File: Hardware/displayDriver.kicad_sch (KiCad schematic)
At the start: 22 parts, among them J3 Conn_01x10, J4 Conn_01x10, U10 4511, U11 HDSP-816E, U12 4511, U13 HDSP-816E, U6 4511, U7 HDSP-816E, U8 4511, U9 HDSP-816E

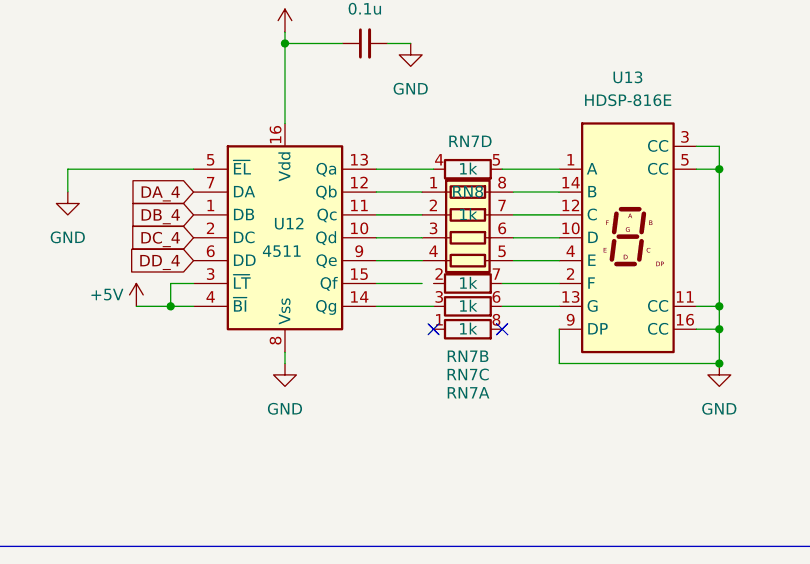
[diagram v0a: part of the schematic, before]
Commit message: Route the 10/hours digits. Update HDSP-816E footprint to include 3D representation
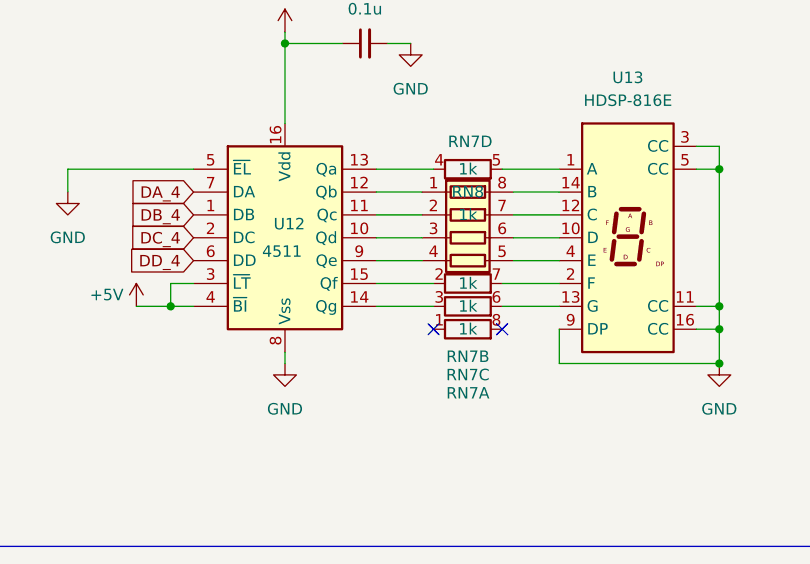
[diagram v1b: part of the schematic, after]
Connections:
- net at U12.15 (Qf): now also RN7.2 (R2.1)
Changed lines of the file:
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@@
 	(wire
 		(pts
-			(xy 78.74 138.43) (xy 83.82 138.43)
+			(xy 78.74 138.43) (xy 85.09 138.43)
 		)
 		(stroke

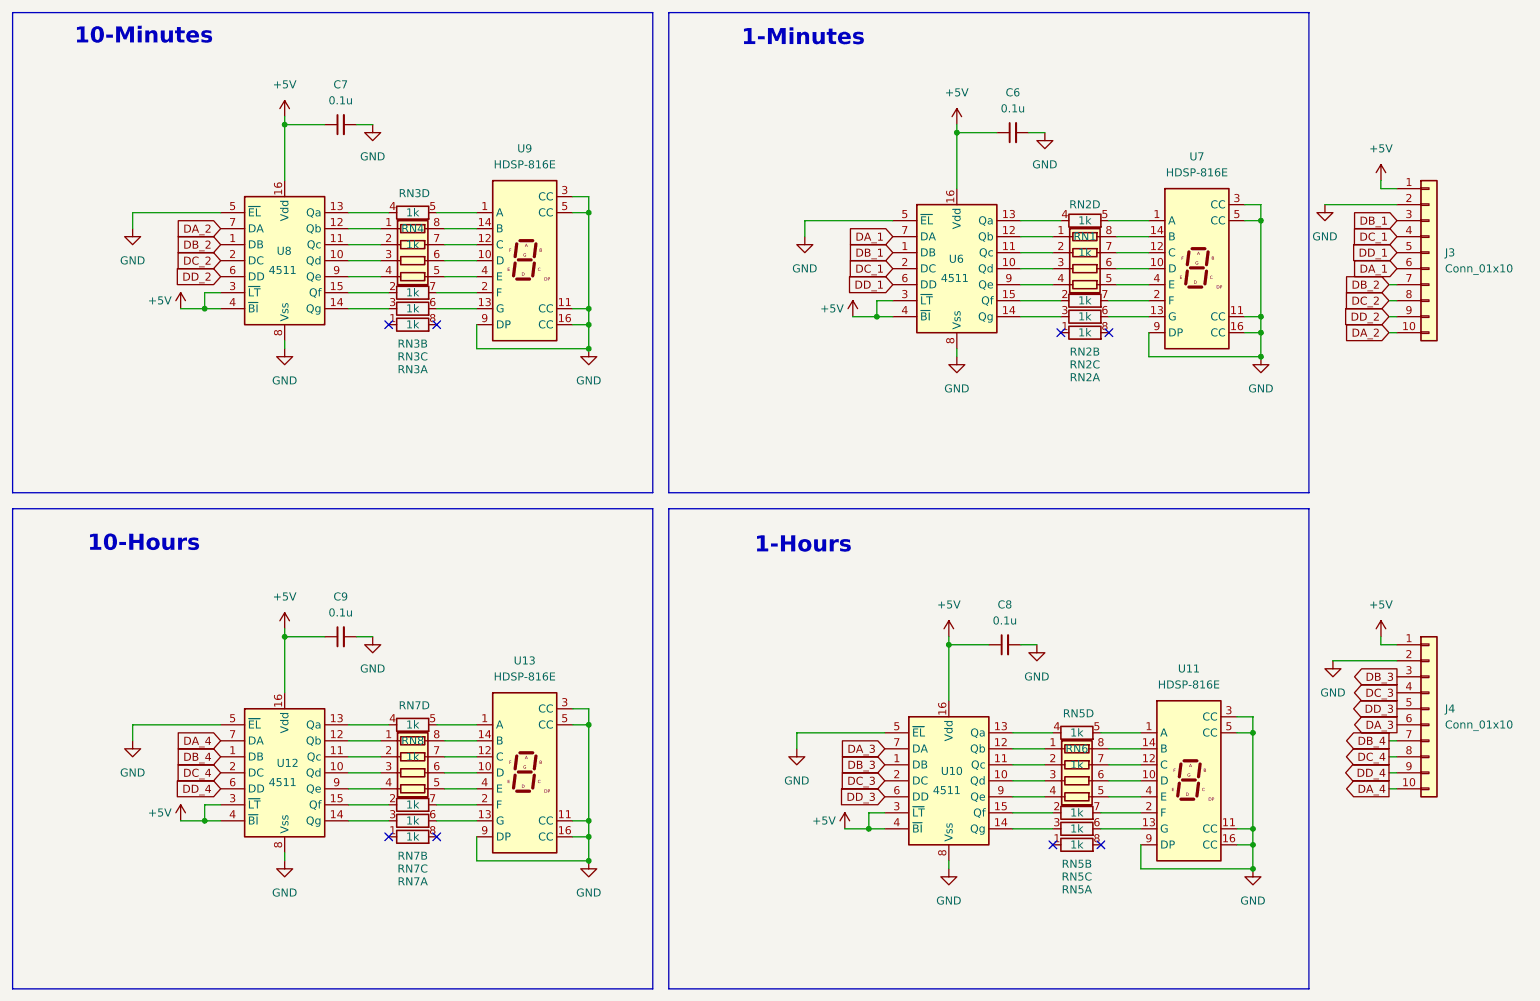
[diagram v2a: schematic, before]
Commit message: Make the IC changes for minute and hour counters
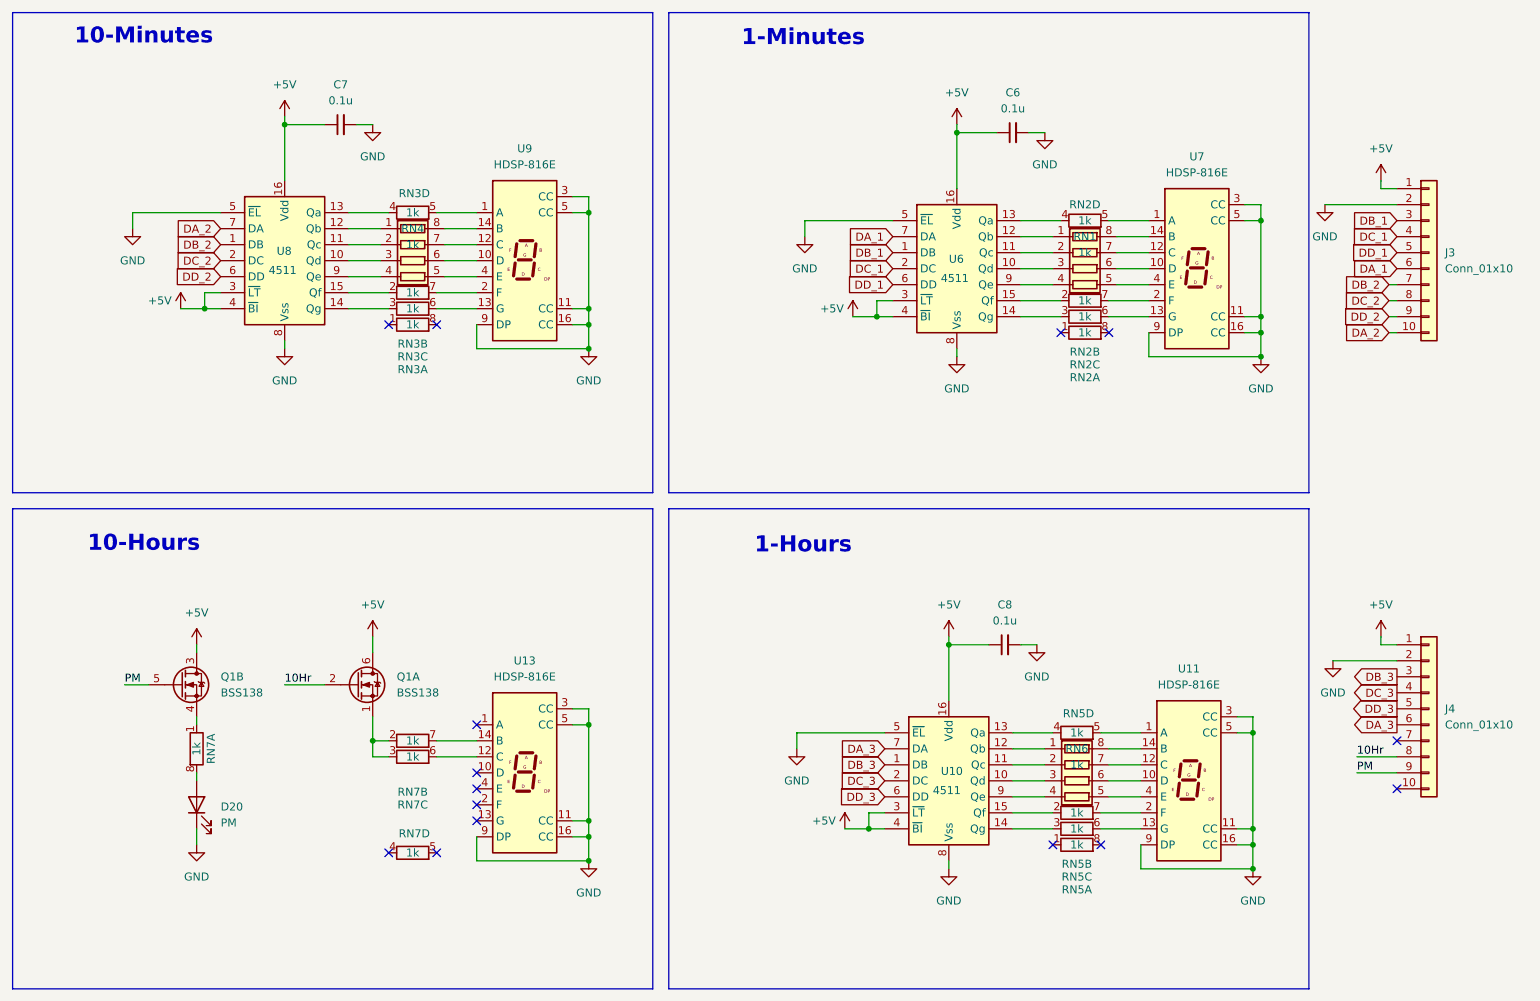
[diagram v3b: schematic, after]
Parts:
- removed C9: 0.1u, Capacitor_SMD:C_0603_1608Metric, symbol Device:C_Small
- removed RN8: 1k, Resistor_SMD:R_Array_Convex_4x0603, symbol Device:R_Pack04
- removed U12: 4511, Package_SO:TSSOP-16_4.4x5mm_P0.65mm, symbol 4xxx_IEEE:4511
- added D20: PM, LED_THT:LED_D5.0mm, symbol Device:LED
- added Q1: BSS138, Package_TO_SOT_SMD:SOT-363, symbol JKC_library:BSS138_dual
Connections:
- net +5V: now also Q1.3 (D2), Q1.6 (D1)
- net GND: now also D20.1 (K)
- net at U13.1 (A): no longer RN7.5 (R4.2)
- net at U13.12 (C): now also RN7.6 (R3.2)
- net at U13.13 (G): no longer RN7.6 (R3.2)
- net at U13.14 (B): now also RN7.7 (R2.2)
- net at U13.2 (F): no longer RN7.7 (R2.2)
- net at RN7.1 (R1.1): now also Q1.4 (S2)
- net at RN7.8 (R1.2): now also D20.2 (A)
- net at RN7.3 (R3.1): now also RN7.2 (R2.1), Q1.1 (S1)
- net DA_4: no longer names the net of J4.10 (Pin_10)
- net DB_4: no longer names the net of J4.7 (Pin_7)
- net DC_4 renamed 10Hr
- net 10Hr: now also Q1.2 (G1)
- net DD_4 renamed PM
- net PM: now also Q1.5 (G2)
- no-connect marks 8 -> 15
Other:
- moved on the sheet: RN7A, RN7B, RN7C

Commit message: Update component symbols and footpints
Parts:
- Q1: footprint Package_TO_SOT_SMD:SOT-363 -> Package_TO_SOT_SMD:SOT-363_SC-70-6
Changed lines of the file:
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@@
 			)
 		)
-		(property "Footprint" "Package_TO_SOT_SMD:SOT-363"
+		(property "Footprint" "Package_TO_SOT_SMD:SOT-363_SC-70-6"
 			(at 57.15 121.285 0)
 			(effects
@@
 			)
 		)
-		(property "Footprint" "Package_TO_SOT_SMD:SOT-363"
+		(property "Footprint" "Package_TO_SOT_SMD:SOT-363_SC-70-6"
 			(at 85.09 121.285 0)
 			(effects

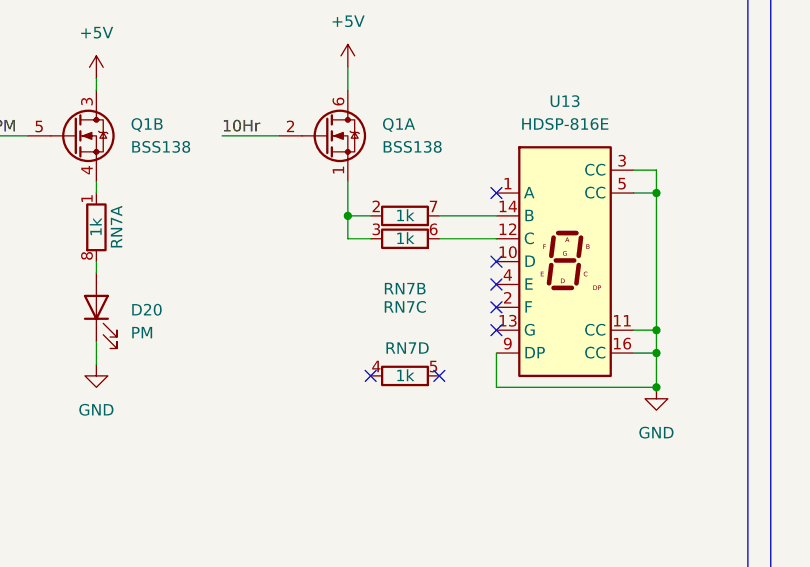
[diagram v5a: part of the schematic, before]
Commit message: Convert layout to 3 board design (power/logic/display)
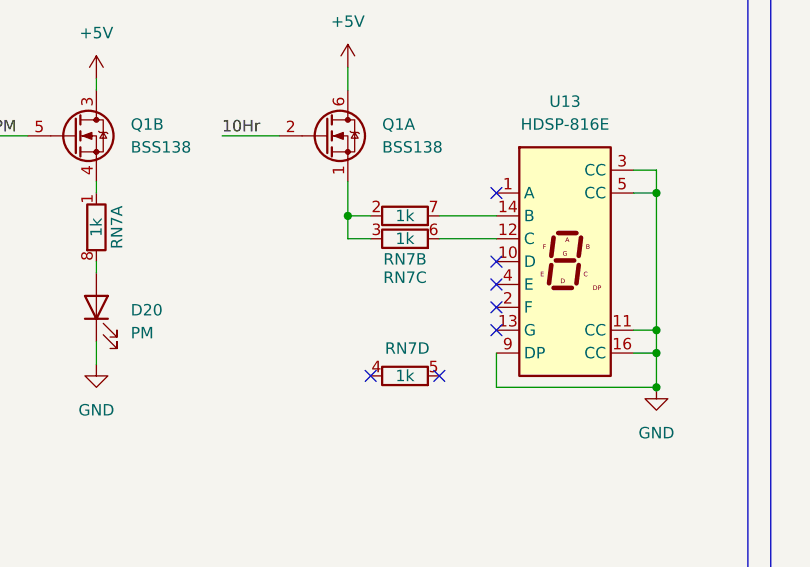
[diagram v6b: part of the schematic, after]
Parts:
- J3, J4: footprint Connector_PinHeader_2.54mm:PinHeader_1x10_P2.54mm_Vertical -> Connector_PinSocket_2.54mm:PinSocket_1x10_P2.54mm_Vertical
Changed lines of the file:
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@@
 			)
 		)
-		(property "Footprint" "Connector_PinHeader_2.54mm:PinHeader_1x10_P2.54mm_Vertical"
+		(property "Footprint" "Connector_PinSocket_2.54mm:PinSocket_1x10_P2.54mm_Vertical"
 			(at 250.19 123.19 0)
 			(effects
@@
 			)
 		)
-		(property "Footprint" "Connector_PinHeader_2.54mm:PinHeader_1x10_P2.54mm_Vertical"
+		(property "Footprint" "Connector_PinSocket_2.54mm:PinSocket_1x10_P2.54mm_Vertical"
 			(at 250.19 50.8 0)
 			(effects
@@
 		(dnp no)
 		(property "Reference" "RN7"
-			(at 88.9 136.398 90)
+			(at 88.9 133.096 90)
 			(effects
 				(font
@@
 		(dnp no)
 		(property "Reference" "RN7"
-			(at 88.9 138.43 90)
-			(effects
-				(font
+			(at 88.9 135.128 90)
+			(effects
+				(font
